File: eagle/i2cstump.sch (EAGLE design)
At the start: 22 parts, among them IC1 ATTINY85, IC2 MCP1703CB, J1 I2C-5V, J2 I2C-3V3, J3 AVR_SPI_PROG_3X2TESTPOINTS, Q1 220mA/50V/3.5Ω, Q2 220mA/50V/3.5Ω, X1 USBPCB

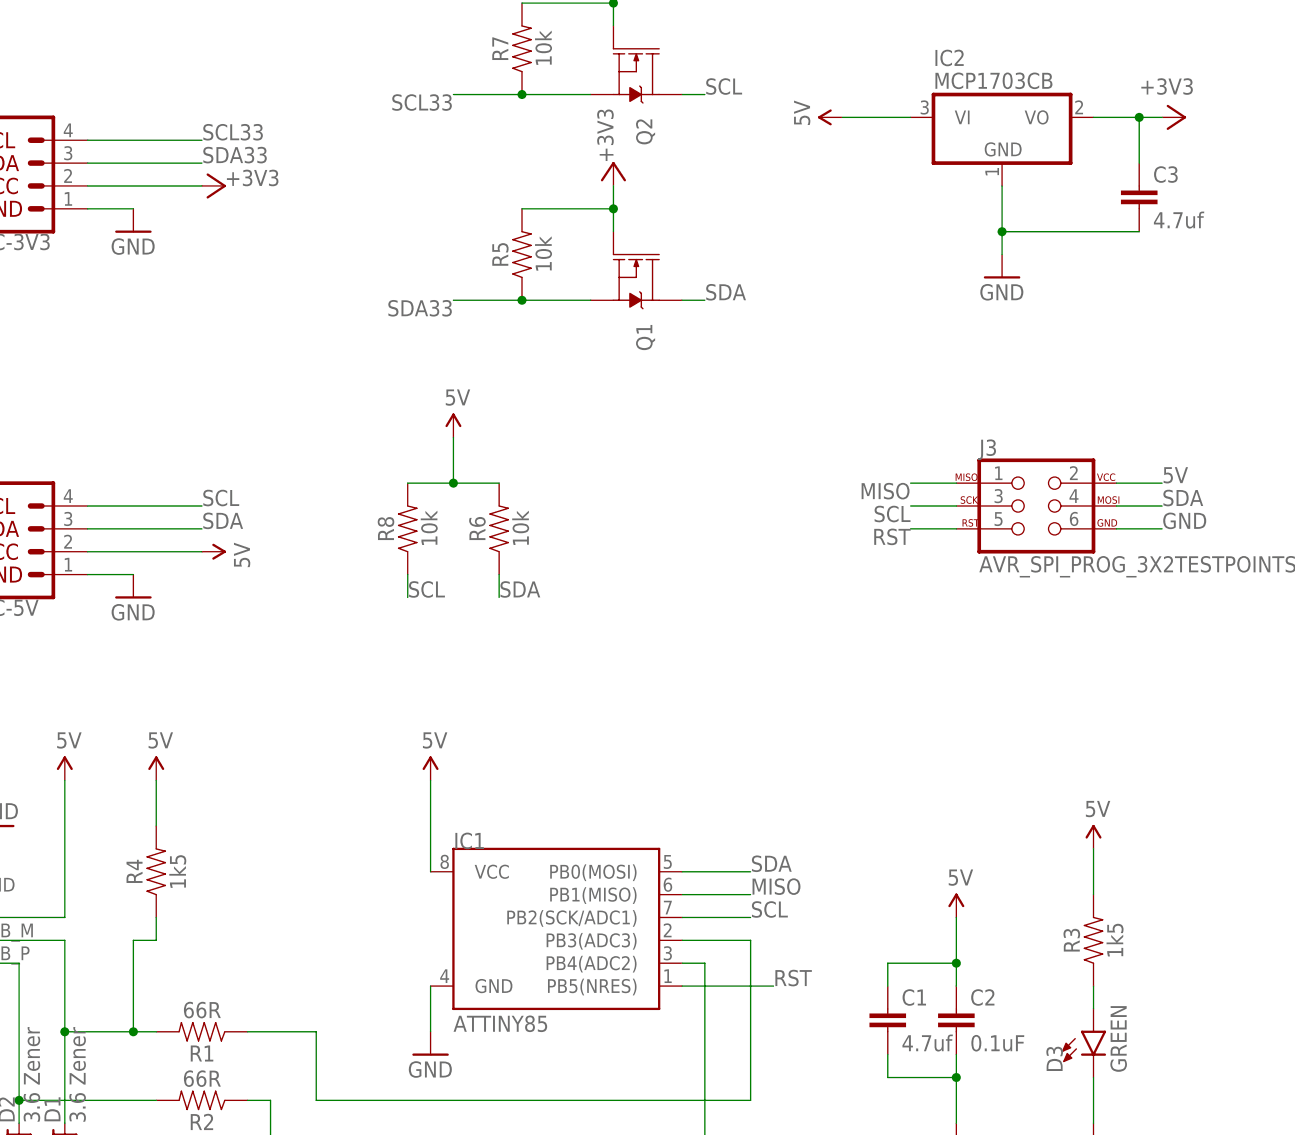
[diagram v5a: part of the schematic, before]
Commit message: Change R3 to 390R, 2.2V green LED, not too bright
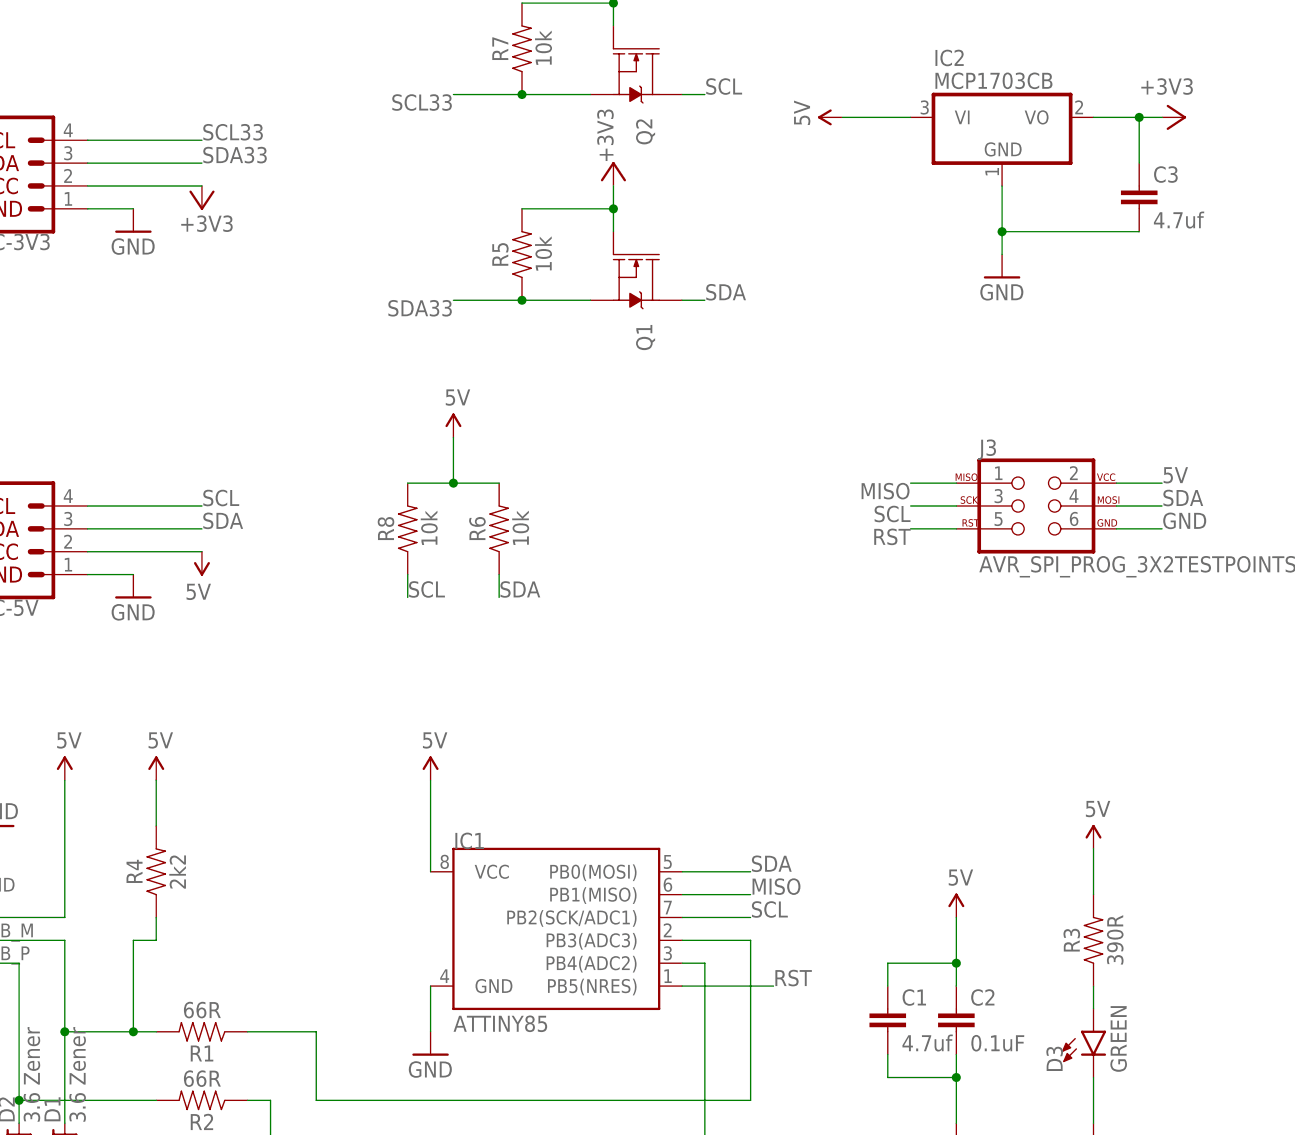
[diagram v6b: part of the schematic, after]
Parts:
- R3: value 1k5 -> 390R
- R4: value 1k5 -> 2k2
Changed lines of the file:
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@@
 <part name="R8" library="SparkFun-Resistors" library_urn="urn:adsk.eagle:library:532" deviceset="RESISTOR" device="0603" package3d_urn="urn:adsk.eagle:package:39650/1" value="10k"/>
 <part name="U$8" library="SparkFun" deviceset="5V" device=""/>
-<part name="R4" library="SparkFun-Resistors" library_urn="urn:adsk.eagle:library:532" deviceset="RESISTOR" device="0603" package3d_urn="urn:adsk.eagle:package:39650/1" value="1k5"/>
+<part name="R4" library="SparkFun-Resistors" library_urn="urn:adsk.eagle:library:532" deviceset="RESISTOR" device="0603" package3d_urn="urn:adsk.eagle:package:39650/1" value="2k2"/>
 <part name="R1" library="SparkFun-Resistors" library_urn="urn:adsk.eagle:library:532" deviceset="RESISTOR" device="0603" package3d_urn="urn:adsk.eagle:package:39650/1" value="66R"/>
 <part name="R2" library="SparkFun-Resistors" library_urn="urn:adsk.eagle:library:532" deviceset="RESISTOR" device="0603" package3d_urn="urn:adsk.eagle:package:39650/1" value="66R"/>
 <part name="C2" library="SparkFun-Capacitors" library_urn="urn:adsk.eagle:library:510" deviceset="0.1UF" device="-0603-25V-(+80/-20%)" package3d_urn="urn:adsk.eagle:package:37414/1" value="0.1uF"/>
 <part name="D3" library="SparkFun-LED" library_urn="urn:adsk.eagle:library:529" deviceset="LED-GREEN" device="0603" package3d_urn="urn:adsk.eagle:package:39354/1" value="GREEN"/>
-<part name="R3" library="SparkFun-Resistors" library_urn="urn:adsk.eagle:library:532" deviceset="RESISTOR" device="0603" package3d_urn="urn:adsk.eagle:package:39650/1" value="1k5"/>
+<part name="R3" library="SparkFun-Resistors" library_urn="urn:adsk.eagle:library:532" deviceset="RESISTOR" device="0603" package3d_urn="urn:adsk.eagle:package:39650/1" value="390R"/>
 <part name="U$9" library="SparkFun" deviceset="5V" device=""/>
 <part name="GND8" library="SparkFun" deviceset="GND" device=""/>
@@
 <attribute name="NAME" x="15.24" y="89.154" size="1.778" layer="95" font="vector"/>
 </instance>
-<instance part="U$4" gate="G$1" x="40.64" y="81.28" smashed="yes" rot="R270">
-<attribute name="VALUE" x="44.196" y="82.296" size="1.778" layer="96" rot="R270"/>
+<instance part="U$4" gate="G$1" x="40.64" y="81.28" smashed="yes" rot="R180">
+<attribute name="VALUE" x="41.656" y="77.724" size="1.778" layer="96" rot="R180"/>
 </instance>
 <instance part="GND4" gate="1" x="33.02" y="76.2" smashed="yes">
@@
 <attribute name="VALUE" x="30.48" y="114.3" size="1.778" layer="96"/>
 </instance>
-<instance part="+3V2" gate="G$1" x="43.18" y="121.92" smashed="yes" rot="R270">
-<attribute name="VALUE" x="43.18" y="121.92" size="1.778" layer="96"/>
+<instance part="+3V2" gate="G$1" x="40.64" y="119.38" smashed="yes" rot="R180">
+<attribute name="VALUE" x="38.1" y="116.84" size="1.778" layer="96"/>
 </instance>
 <instance part="Q1" gate="NMOS" x="88.9" y="111.76" smashed="yes" rot="R270">

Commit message: Version 4.0
Changes:
- swap out PWR led for ACT led on MISO pin (the USB Tiny I2C firmware
blinks MISO on I2C activity.
- swap out 10KOhm pullup resistors for an 0805 resistor network RN1.
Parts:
- removed J3: AVR_SPI_PROG_3X2TESTPOINTS, SparkFun-Connectors:AVR_SPI_PROG_3X2TESTPOINTS
- removed R5, R6, R7, R8: 10k, SparkFun-Resistors:RESISTOR0603
- added RN1: CTS742C083, resistor-net:CTS742C083
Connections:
- net +3V3: now also RN1.5, RN1.6; no longer R5.2, R7.2
- net 5V: now also RN1.7, RN1.8; no longer J3.2, R3.2, R6.2, R8.2
- net GND: no longer J3.6
- net MISO: now also R3.2; no longer J3.1
- net RST: no longer J3.5
- net SCL: now also RN1.1; no longer J3.3, R8.1
- net SCL33: now also RN1.3; no longer R7.1
- net SDA: now also RN1.2; no longer J3.4, R6.1
- net SDA33: now also RN1.4; no longer R5.1
